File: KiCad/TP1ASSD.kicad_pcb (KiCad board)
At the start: 2 copper layers, 200 x 50 mm, 87 parts, among them J1 Alimentacion, J10 JumperCtrlAS, J11 JumperCtrlSH, J2 GND, J3 Vi, J4 Jumper_FA, J5 Jumper_SH, J6 Jumper_AS, J7 Jumper_AS, J8 Vo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

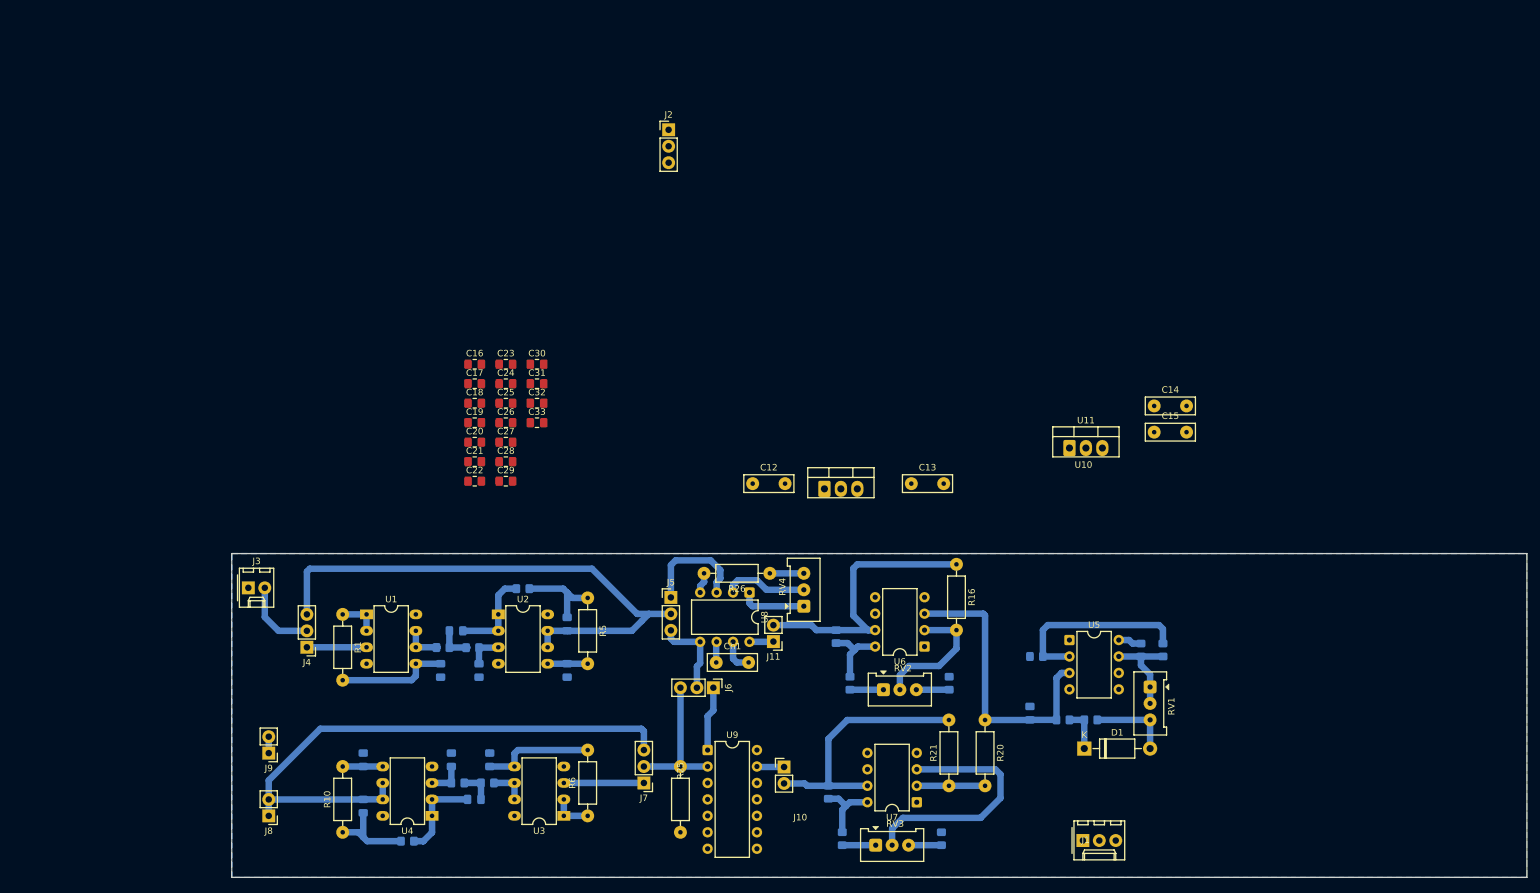
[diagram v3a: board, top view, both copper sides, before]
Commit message: Empece a rutear la alimentacion
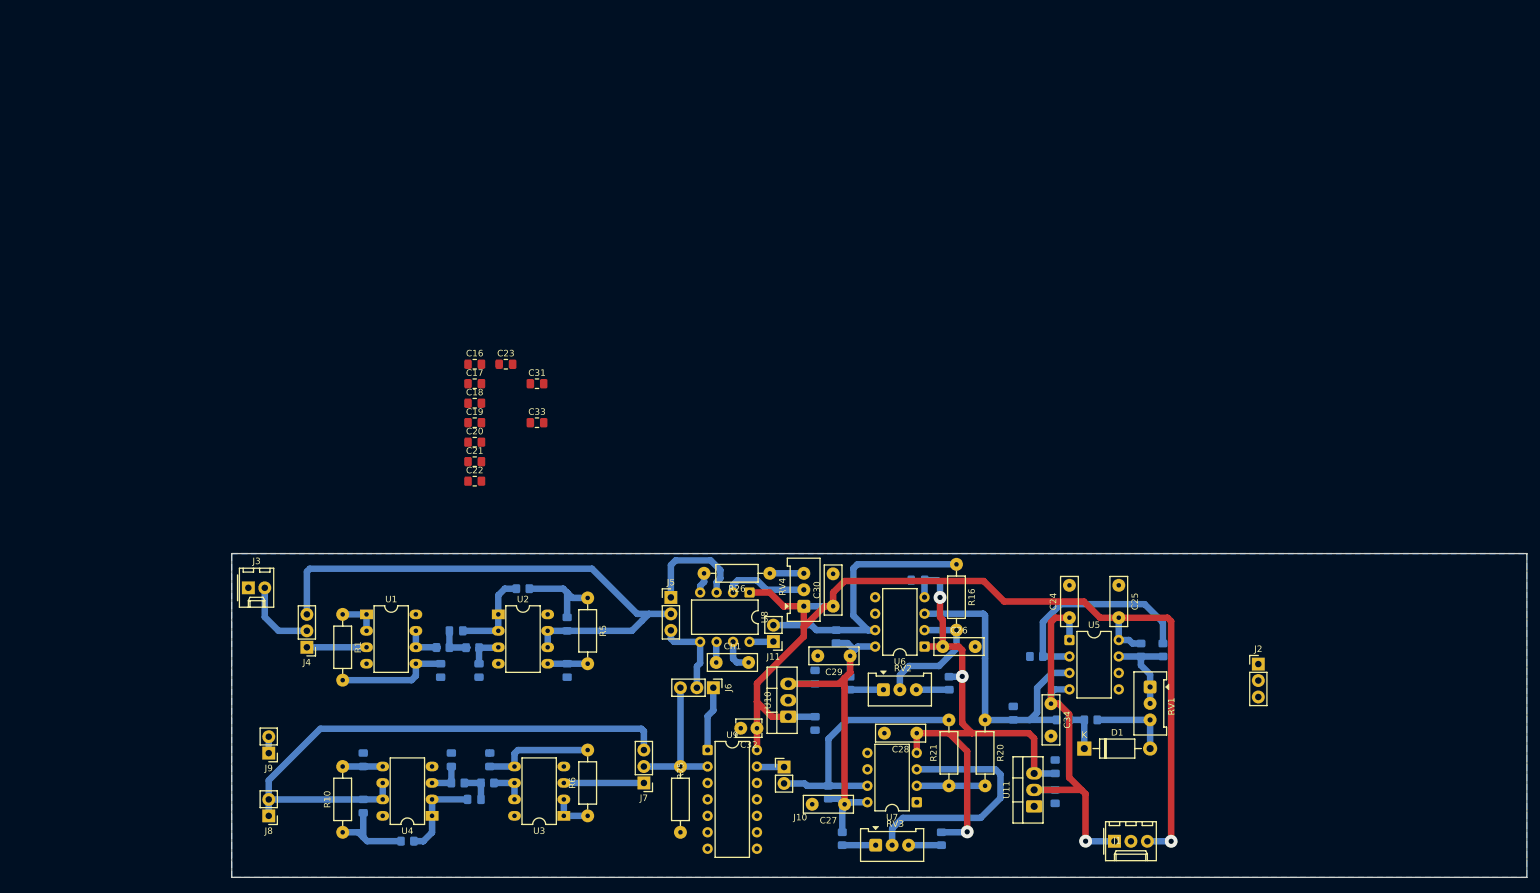
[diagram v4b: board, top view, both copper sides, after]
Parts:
- added C34: 100n, TCLib:C_5mm, F.Cu at (179.6, 124.5)
- added C35: 100n, TCLib:C_0805, B.Cu at (159.0, 105.4)
- C12, C13, C14, C15: footprint TCLib:C_5mm -> TCLib:C_0805; moved to B.Cu
- C24, C25, C26, C27, C28, C29, C30: footprint TCLib:C_0805 -> TCLib:C_5mm
- C32: footprint TCLib:C_0805 -> TCLib:C_2.5mm
- moved J2 122.9 mm to (211.6, 118.4)
- moved C25 98.7 mm to (190.0, 106.2), turned to -90 degrees
- moved C24 94.2 mm to (182.4, 111.2), turned to 90 degrees
- moved C27 76.6 mm to (147.7, 140.0), turned to 180 degrees
- moved C28 76.1 mm to (158.8, 129.0), turned to 180 degrees
- moved C26 75.8 mm to (162.9, 115.7)
- moved C14 62.2 mm to (180.2, 138.8), turned to -90 degrees
- moved C32 60.6 mm to (134.2, 128.3), turned to 180 degrees
- moved C29 59.6 mm to (148.6, 117.1), turned to 180 degrees
- moved C30 59.1 mm to (145.9, 109.4), turned to 90 degrees
- moved U11 55.6 mm to (177.0, 140.3), turned to 90 degrees
- moved C15 53.9 mm to (180.2, 134.2), turned to 90 degrees
- moved C12 38.3 mm to (143.1, 127.5), turned to -90 degrees
- moved U10 35.6 mm to (139.0, 126.5), turned to 90 degrees
- moved C13 33.4 mm to (143.1, 120.4), turned to 90 degrees
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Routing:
- net +10V: track 13.9 -> 157.2 mm, vias 0 -> 1
- net -5V: track 0.00 -> 87.3 mm, vias 0 -> 3
- net -10V: track 3.22 -> 66.3 mm, vias 0 -> 1
- net +5V: track 22.1 -> 58.6 mm
- net Net-(U5-+): track 29.5 -> 33.5 mm
- net Net-(U5--): track 45.4 -> 48.0 mm

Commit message: Termine alimentacion
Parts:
- C16, C17, C18, C19, C20, C21, C22, C23, C31, C33: footprint TCLib:C_0805 -> TCLib:C_5mm
- moved J2 97.3 mm to (114.2, 118.2)
- moved C33 69.7 mm to (123.3, 146.9), turned to 180 degrees
- moved C20 61.6 mm to (96.7, 145.4)
- moved C22 59.7 mm to (76.4, 148.1), turned to 180 degrees
- moved C23 54.9 mm to (84.0, 125.8), turned to -90 degrees
- moved C17 46.6 mm to (89.2, 121.7)
- moved C19 43.0 mm to (78.9, 122.5), turned to 180 degrees
- moved C21 40.3 mm to (104.4, 125.0), turned to -90 degrees
- moved C31 36.8 mm to (122.5, 104.3), turned to 180 degrees
- moved C16 36.4 mm to (81.5, 107.3)
- moved C18 31.5 mm to (106.3, 105.4)
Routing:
- net -10V: track 66.3 -> 275.3 mm
- net +10V: track 157.2 -> 316.4 mm
- net GND: track 7.94 -> 26.1 mm, vias 0 -> 2
- net /SH_ctrl: track 43.8 -> 44.4 mm

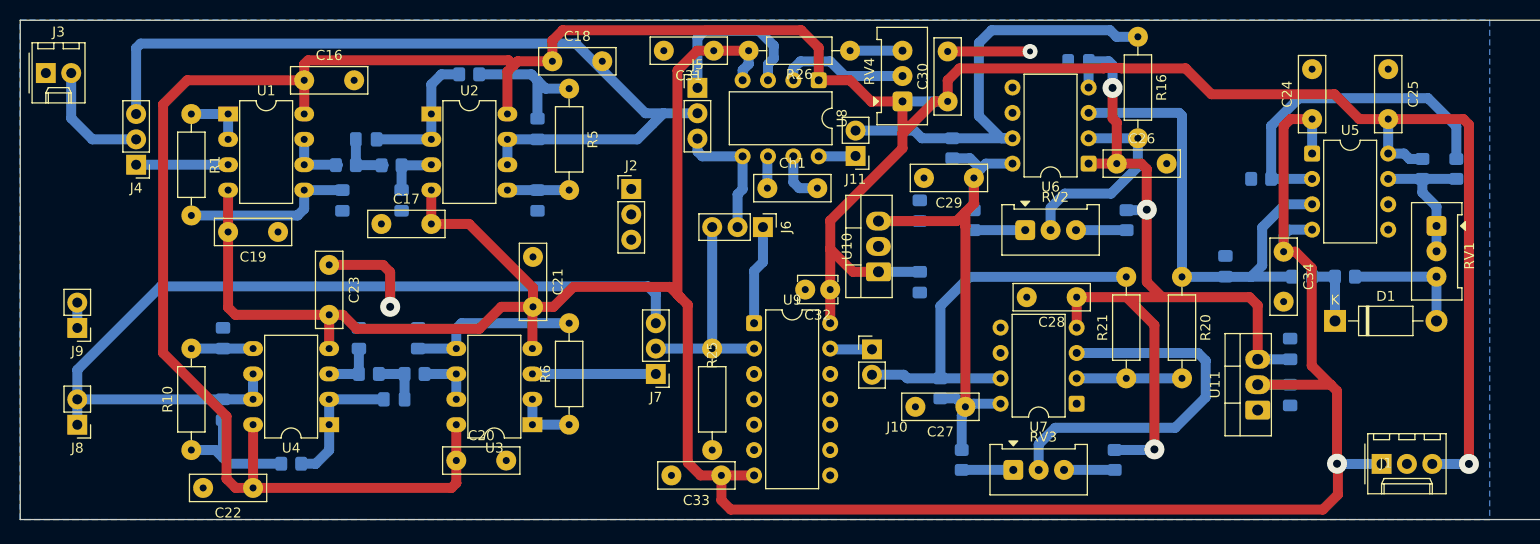
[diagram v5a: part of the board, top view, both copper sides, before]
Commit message: Front silkscreen text size increased
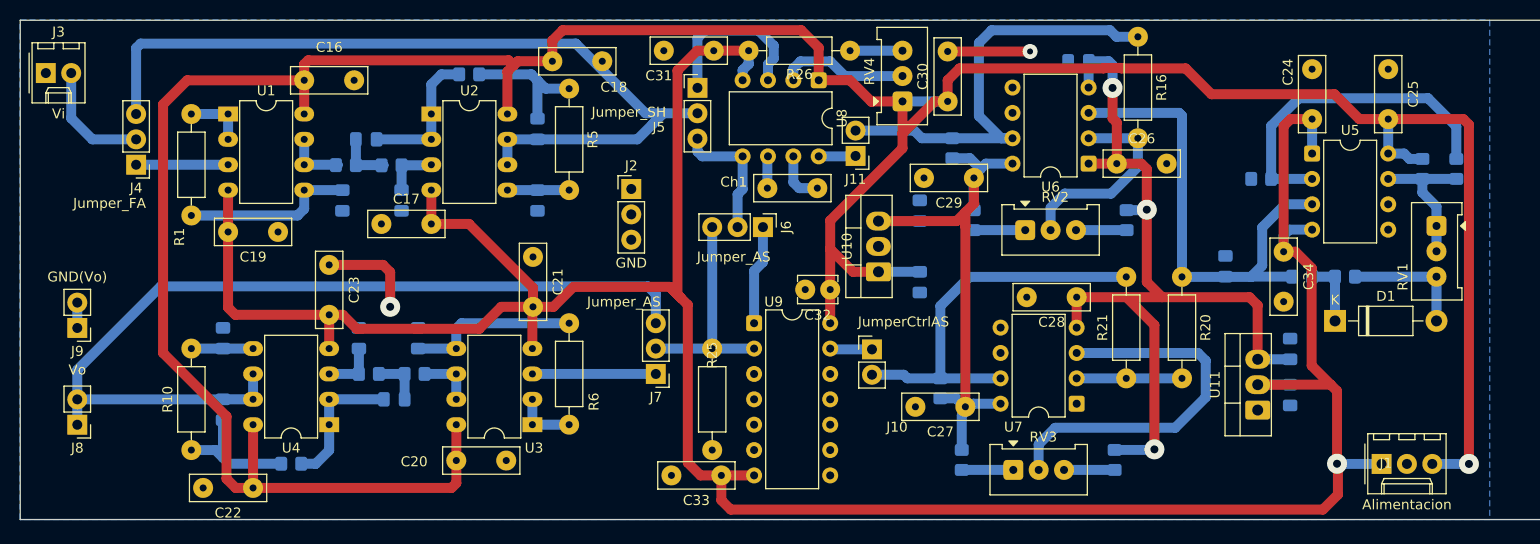
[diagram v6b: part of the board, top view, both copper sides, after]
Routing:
- net -10V: track 275.3 -> 276.6 mm
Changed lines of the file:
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@@
 		(tags "Resistor Axial_DIN0207 series Axial Horizontal pin pitch 10.16mm 0.25W = 1/4W length 6.3mm diameter 2.5mm")
 		(property "Reference" "R1"
-			(at 5.08 -2.37 90)
+			(at 12.3075 1.19 90)
 			(layer "F.SilkS")
 			(effects
@@
 		(tags "C Disc series Radial pin pitch 5.00mm  diameter 7.5mm width 2.5mm Capacitor")
 		(property "Reference" "Ch1"
-			(at 2.5 -2.5 0)
+			(at -3.37 -0.615 0)
 			(layer "F.SilkS")
 			(effects
@@
 		(tags "Through hole pin header THT 1x03 2.54mm single row")
 		(property "Reference" "J5"
-			(at 0 -2.33 0)
+			(at -3.87 3.925 0)
 			(layer "F.SilkS")
 			(effects
@@
 		)
 		(property "Value" "Jumper_SH"
-			(at 2.11 7.55 0)
-			(layer "F.Fab")
+			(at -6.87 2.425 0)
+			(layer "F.SilkS")
 			(effects
 				(font
@@
 		(tags "Resistor Axial_DIN0207 series Axial Horizontal pin pitch 10.16mm 0.25W = 1/4W length 6.3mm diameter 2.5mm")
 		(property "Reference" "R6"
-			(at 5.08 -2.37 90)
+			(at 2.3 2.48 90)
 			(layer "F.SilkS")
 			(effects
@@
 		)
 		(property "Value" "JumperCtrlSH"
-			(at -1.5 6.37 0)
+			(at -6.8 1.39 0)
 			(layer "F.Fab")
 			(effects
@@
 		(tags "C Disc series Radial pin pitch 5.00mm  diameter 7.5mm width 2.5mm Capacitor")
 		(property "Reference" "C20"
-			(at 2.5 -2.5 0)
+			(at -4.22 0.1104 0)
 			(layer "F.SilkS")
 			(effects
@@
 		(tags "THT DIP DIL PDIP 2.54mm 7.62mm 300mil")
 		(property "Reference" "U9"
-			(at 3.81 -2.33 0)
+			(at 1.96 -2.14 0)
 			(layer "F.SilkS")
 			(effects
@@
 		(tags "C Disc series Radial pin pitch 5.00mm  diameter 7.5mm width 2.5mm Capacitor")
 		(property "Reference" "C16"
-			(at 2.5 -2.5 0)
+			(at 2.51 -3.315 0)
 			(layer "F.SilkS")
 			(effects
@@
 		(property "Value" "GND"
 			(at 0 7.41 0)
-			(layer "F.Fab")
+			(layer "F.SilkS")
 			(effects
 				(font
@@
 		(tags "C Disc series Radial pin pitch 5.00mm  diameter 7.5mm width 2.5mm Capacitor")
 		(property "Reference" "C24"
-			(at 2.5 -2.5 90)
+			(at 4.7 -2.415 90)
 			(layer "F.SilkS")
 			(effects
@@
 		)
 		(property "Value" "100n"
-			(at 2.5 2.5 0)
+			(at -1.13 -2.5 0)
 			(layer "F.Fab")
 			(effects
@@
 		(tags "C Disc series Radial pin pitch 5.00mm  diameter 7.5mm width 2.5mm Capacitor")
 		(property "Reference" "C18"
-			(at 2.5 -2.5 0)
+			(at 6.161 2.59 0)
 			(layer "F.SilkS")
 			(effects
@@
 		)
 		(property "Value" "Vo"
-			(at 0 4.87 0)
-			(layer "F.Fab")
+			(at 0 5.495 0)
+			(layer "F.SilkS")
 			(effects
 				(font
@@
 		)
 		(property "Value" "Jumper_AS"
-			(at 0 7.41 90)
-			(layer "F.Fab")
+			(at 2.985 2.925 0)
+			(layer "F.SilkS")
 			(effects
 				(font
@@
 		)
 		(property "Value" "82k"
-			(at 5.08 2.37 90)
+			(at 8.84 -2.69 90)
 			(layer "F.Fab")
 			(effects
@@
 		)
 		(property "Value" "Jumper_FA"
-			(at 0.33 -3.86 0)
-			(layer "F.Fab")
+			(at 2.66 -3.86 0)
+			(layer "F.SilkS")
 			(effects
 				(font
@@
 		(tags "Potentiometer ")
 		(property "Reference" "RV1"
-			(at 3 -3.3 90)
+			(at 5.1 3.37 90)
 			(layer "F.SilkS")
 			(effects
@@
 		)
 		(property "Value" "Jumper_AS"
-			(at 0 7.41 0)
-			(layer "F.Fab")
+			(at 3.2 7.22 0)
+			(layer "F.SilkS")
 			(effects
 				(font
@@
 		)
 		(property "Value" "LM79xx"
-			(at 2.54 2.5 90)
+			(at 2.335 2.5 90)
 			(layer "F.Fab")
 			(effects
@@
 		(tags "Potentiometer ")
 		(property "Reference" "RV3"
-			(at 3 -3.3 0)
+			(at 3.005 -3.3 0)
 			(layer "F.SilkS")
 			(effects
@@
 		(tags "THT DIP DIL PDIP 2.54mm 7.62mm 300mil")
 		(property "Reference" "U7"
-			(at 3.81 -2.33 0)
+			(at 6.34 -2.33 0)
 			(layer "F.SilkS")
 			(effects
@@
 		(tags "C Disc series Radial pin pitch 5.00mm  diameter 7.5mm width 2.5mm Capacitor")
 		(property "Reference" "C31"
-			(at 2.5 -2.5 0)
+			(at 5.5 -2.5 0)
 			(layer "F.SilkS")
 			(effects
@@
 		(property "Value" "Alimentacion"
 			(at 2.54 4.08 0)
-			(layer "F.Fab")
+			(layer "F.SilkS")
 			(effects
 				(font
@@
 		(tags "THT DIP DIL PDIP 2.54mm 7.62mm 300mil")
 		(property "Reference" "U3"
-			(at 3.81 -2.33 0)
+			(at -0.16 -2.33 0)
 			(layer "F.SilkS")
 			(effects
@@
 		(property "Value" "Vi"
 			(at 1.27 4.08 0)
-			(layer "F.Fab")
+			(layer "F.SilkS")
 			(effects
 				(font
@@
 		)
 		(property "Value" "JumperCtrlAS"
-			(at 0 4.87 0)
-			(layer "F.Fab")
+			(at 3.155 -2.76 0)
+			(layer "F.SilkS")
 			(effects
 				(font
@@
 		)
 		(property "Value" "GND(Vo)"
-			(at 0 4.87 0)
-			(layer "F.Fab")
+			(at 0 5.115 0)
+			(layer "F.SilkS")
 			(effects
 				(font
@@
 	)
 	(segment
-		(start 106.45 130)
-		(end 108.45 128)
+		(start 120.85 104.35)
+		(end 122.5 104.35)
 		(width 1)
 		(layer "F.Cu")
@@
 	)
 	(segment
-		(start 119.9 129.8)
-		(end 119.9 145.6)
+		(start 121.18 146.88)
+		(end 123.2624 146.88)
 		(width 1)
 		(layer "F.Cu")
@@
 	)
 	(segment
-		(start 118.869 106.331)
-		(end 120.85 104.35)
+		(start 118.869 128.769)
+		(end 118.869 106.331)
+		(width 1)
+		(layer "F.Cu")
+		(net 19)
+	)
+	(segment
+		(start 119.9 145.6)
+		(end 121.18 146.88)
 		(width 1)
 		(layer "F.Cu")
@@
 	)
 	(segment
-		(start 119.2 129.1)
-		(end 118.869 128.769)
+		(start 104.4 130)
+		(end 106.45 130)
 		(width 1)
 		(layer "F.Cu")
@@
 	)
 	(segment
-		(start 98 121.7)
-		(end 94.22 121.7)
+		(start 118.3 128.2)
+		(end 119.9 129.8)
 		(width 1)
 		(layer "F.Cu")
@@
 	)
 	(segment
-		(start 180.741 124.48)
-		(end 179.565 124.48)
+		(start 98 121.7)
+		(end 94.22 121.7)
 		(width 1)
 		(layer "F.Cu")
@@
 	)
 	(segment
-		(start 118.869 128.769)
-		(end 118.869 106.331)
+		(start 180.741 124.48)
+		(end 179.565 124.48)
 		(width 1)
 		(layer "F.Cu")
@@
 	)
 	(segment
-		(start 121.18 146.88)
-		(end 123.2624 146.88)
-		(width 1)
-		(layer "F.Cu")
-		(net 19)
-	)
-	(segment
 		(start 86.75 132.2)
 		(end 99.025 132.2)
@@
 	)
 	(segment
-		(start 119.9 145.6)
-		(end 121.18 146.88)
+		(start 123.2624 146.88)
+		(end 126.54 146.88)
 		(width 1)
 		(layer "F.Cu")
@@
 	)
 	(segment
-		(start 123.2624 146.88)
-		(end 126.54 146.88)
+		(start 106.45 130)
+		(end 108.45 128)
+		(width 1)
+		(layer "F.Cu")
+		(net 19)
+	)
+	(segment
+		(start 108.45 128)
+		(end 118.1 128)
 		(width 1)
 		(layer "F.Cu")
@@
 	)
 	(segment
-		(start 83.99 134.18)
-		(end 83.99 130.8)
+		(start 118.869 106.331)
+		(end 120.85 104.35)
 		(width 1)
 		(layer "F.Cu")
@@
 	)
 	(segment
-		(start 118.1 128)
-		(end 119.2 129.1)
+		(start 119.2 129.1)
+		(end 118.869 128.769)
+		(width 1)
+		(layer "F.Cu")
+		(net 19)
+	)
+	(segment
+		(start 83.99 134.18)
+		(end 83.99 130.8)
 		(width 1)
 		(layer "F.Cu")
@@
 	)
 	(segment
-		(start 104.4 130)
-		(end 106.45 130)
+		(start 118.1 128)
+		(end 119.2 129.1)
 		(width 1)
 		(layer "F.Cu")
@@
 	)
 	(segment
-		(start 120.85 104.35)
-		(end 122.5 104.35)
+		(start 119.9 129.8)
+		(end 119.9 145.6)
 		(width 1)
 		(layer "F.Cu")
@@
 	)
 	(segment
-		(start 108.45 128)
-		(end 118.1 128)
-		(width 1)
-		(layer "F.Cu")
-		(net 19)
-	)
-	(segment
 		(start 184.912 145.71)
 		(end 184.912 138.43)
 		(width 1)
 		(layer "F.Cu")
-		(net 19)
-	)
-	(segment
-		(start 119.2 129.1)
-		(end 119.9 129.8)
-		(width 1)
-		(layer "F.Cu")
